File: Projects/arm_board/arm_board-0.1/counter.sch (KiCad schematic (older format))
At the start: 4 parts, among them U1 74HC193, U2 74HC193, U3 74HC193, U4 74HC193

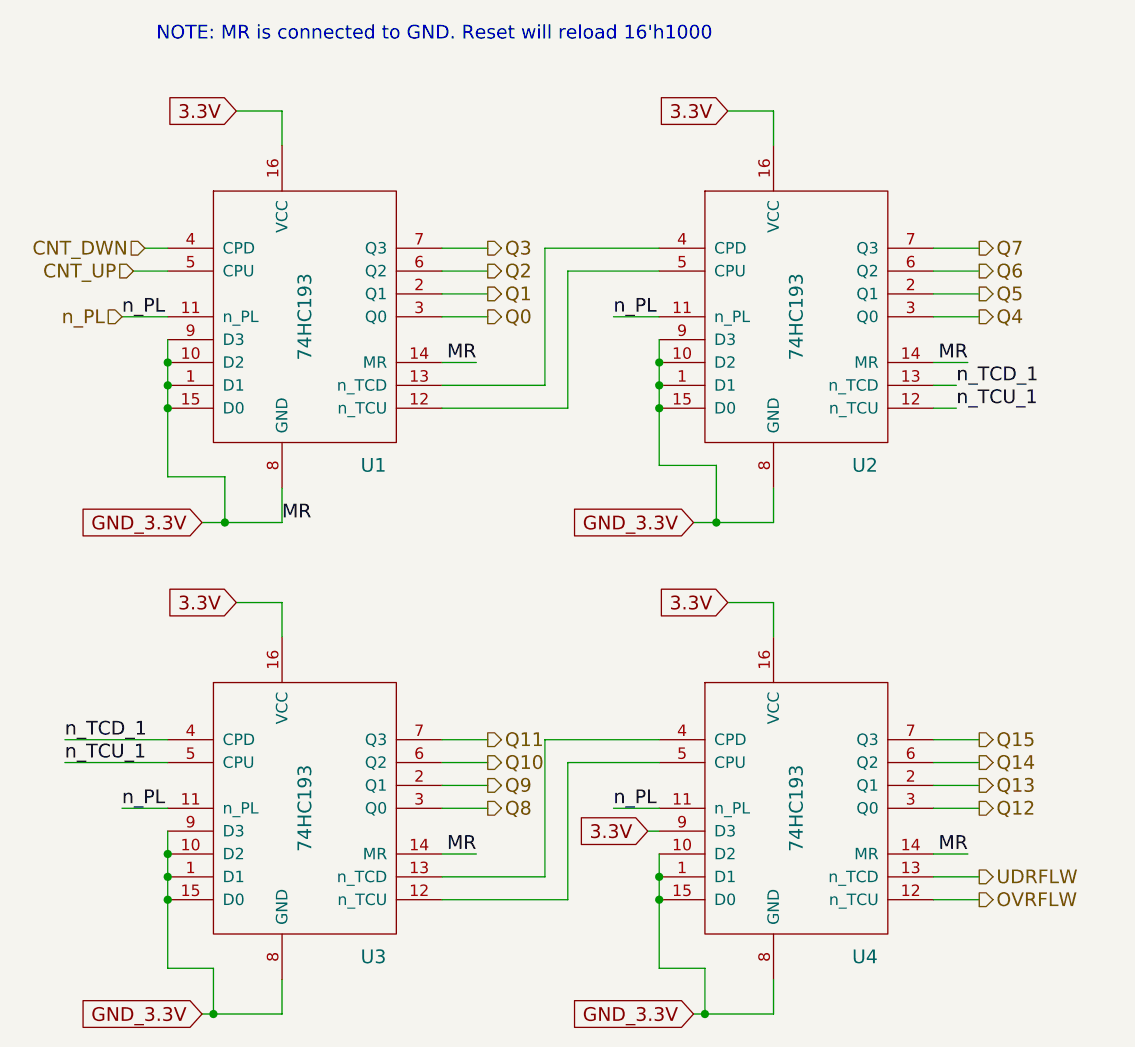
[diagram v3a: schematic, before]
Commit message: Arm Board: bug fixes, and added footprints
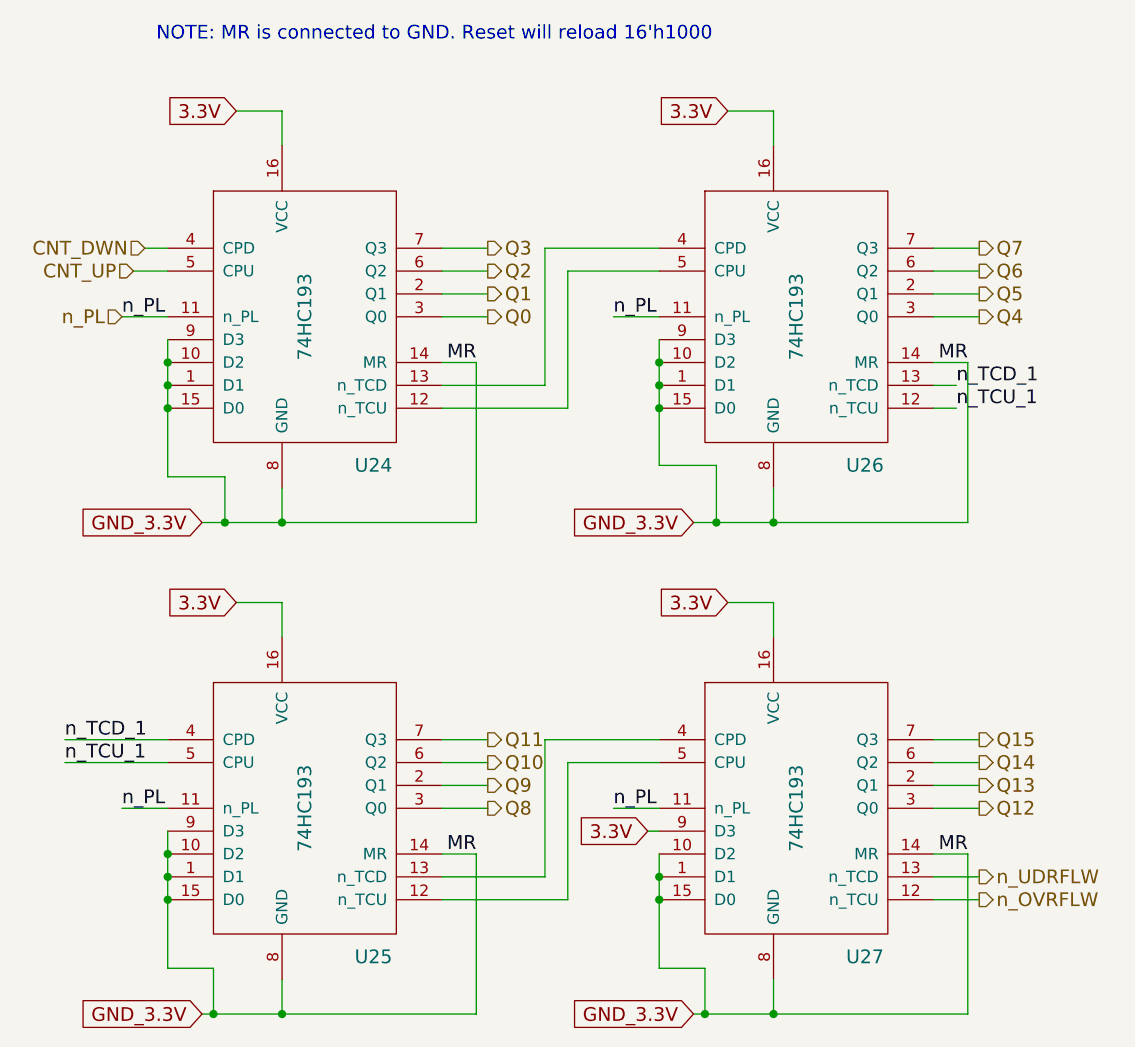
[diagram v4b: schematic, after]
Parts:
- U17: renamed from U1; footprint (none) -> SMD_Packages:SO-16-N
- U18: renamed from U3; footprint (none) -> SMD_Packages:SO-16-N
- U19: renamed from U2; footprint (none) -> SMD_Packages:SO-16-N
- U20: renamed from U4; footprint (none) -> SMD_Packages:SO-16-N
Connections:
- net OVRFLW renamed n_OVRFLW
- net UDRFLW renamed n_UDRFLW
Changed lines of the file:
@@
 LIBS:ArmComponentLibrary
 LIBS:arm_board-cache
-EELAYER 27 0
+EELAYER 25 0
 EELAYER END
 $Descr A4 11693 8268
@@
 $EndDescr
 $Comp
-L 74HC193 U1
+L 74HC193 U17
 U 1 1 564D42F4
 P 4500 2250
-AR Path="/564B31DF/564A908F/564D3AE9/564D42F4" Ref="U1"  Part="1"
-AR Path="/564B31DF/564A908F/564EF627/564D42F4" Ref="U1"  Part="1"
-AR Path="/56666F75/564A908F/564D3AE9/564D42F4" Ref="U1"  Part="1"
-AR Path="/56669634/564A908F/564D3AE9/564D42F4" Ref="U1"  Part="1"
-AR Path="/56669644/564A908F/564D3AE9/564D42F4" Ref="U1"  Part="1"
-AR Path="/5666D2E0/564A908F/564D3AE9/564D42F4" Ref="U1"  Part="1"
-AR Path="/5666D2F0/564A908F/564D3AE9/564D42F4" Ref="U1"  Part="1"
-AR Path="/56F53B7D/564A908F/564D3AE9/564D42F4" Ref="U1"  Part="1"
-AR Path="/56F75F1F/564A908F/564D3AE9/564D42F4" Ref="U1"  Part="1"
-F 0 "U1" H 4800 1600 60  0000 C CNN
+AR Path="/56F5245F/564A908F/564D3AE9/564D42F4" Ref="U17"  Part="1"
+AR Path="/56F53B7D/564A908F/564D3AE9/564D42F4" Ref="U24"  Part="1"
+AR Path="/56F544AF/564A908F/564D3AE9/564D42F4" Ref="U31"  Part="1"
+AR Path="/56F55E0D/564A908F/564D3AE9/564D42F4" Ref="U38"  Part="1"
+AR Path="/56F56B2F/564A908F/564D3AE9/564D42F4" Ref="U45"  Part="1"
+AR Path="/56F75F1F/56AED673/564D3AE9/564D42F4" Ref="U52"  Part="1"
+F 0 "U24" H 4800 1600 60  0000 C CNN
 F 1 "74HC193" V 4500 2250 60  0000 C CNN
-F 2 "" H 4500 2050 60  0000 C CNN
+F 2 "SMD_Packages:SO-16-N" H 4500 2050 60  0001 C CNN
 F 3 "" H 4500 2050 60  0000 C CNN
 	1    4500 2250
@@
 GND_3.3V
 Wire Wire Line
-	4050 3150 4400 3150
+	4050 3150 5250 3150
 Wire Wire Line
 	4400 3150 4400 3000
@@
 	4400 1350 4400 1500
 $Comp
-L 74HC193 U2
+L 74HC193 U19
 U 1 1 564D42F6
 P 6650 2250
-AR Path="/564B31DF/564A908F/564D3AE9/564D42F6" Ref="U2"  Part="1"
-AR Path="/564B31DF/564A908F/564EF627/564D42F6" Ref="U2"  Part="1"
-AR Path="/56666F75/564A908F/564D3AE9/564D42F6" Ref="U2"  Part="1"
-AR Path="/56669634/564A908F/564D3AE9/564D42F6" Ref="U2"  Part="1"
-AR Path="/56669644/564A908F/564D3AE9/564D42F6" Ref="U2"  Part="1"
-AR Path="/5666D2E0/564A908F/564D3AE9/564D42F6" Ref="U2"  Part="1"
-AR Path="/5666D2F0/564A908F/564D3AE9/564D42F6" Ref="U2"  Part="1"
-AR Path="/56F53B7D/564A908F/564D3AE9/564D42F6" Ref="U2"  Part="1"
-AR Path="/56F75F1F/564A908F/564D3AE9/564D42F6" Ref="U2"  Part="1"
-F 0 "U2" H 6950 1600 60  0000 C CNN
+AR Path="/56F5245F/564A908F/564D3AE9/564D42F6" Ref="U19"  Part="1"
+AR Path="/56F53B7D/564A908F/564D3AE9/564D42F6" Ref="U26"  Part="1"
+AR Path="/56F544AF/564A908F/564D3AE9/564D42F6" Ref="U33"  Part="1"
+AR Path="/56F55E0D/564A908F/564D3AE9/564D42F6" Ref="U40"  Part="1"
+AR Path="/56F56B2F/564A908F/564D3AE9/564D42F6" Ref="U47"  Part="1"
+AR Path="/56F75F1F/56AED673/564D3AE9/564D42F6" Ref="U54"  Part="1"
+F 0 "U26" H 6950 1600 60  0000 C CNN
 F 1 "74HC193" V 6650 2250 60  0000 C CNN
-F 2 "" H 6650 2050 60  0000 C CNN
+F 2 "SMD_Packages:SO-16-N" H 6650 2050 60  0001 C CNN
 F 3 "" H 6650 2050 60  0000 C CNN
 	1    6650 2250
@@
 GND_3.3V
 Wire Wire Line
-	6200 3150 6550 3150
+	6200 3150 7400 3150
 Wire Wire Line
 	6550 3150 6550 3000
@@
 	5550 1950 6050 1950
 $Comp
-L 74HC193 U3
+L 74HC193 U18
 U 1 1 564D42F7
 P 4500 4400
-AR Path="/564B31DF/564A908F/564D3AE9/564D42F7" Ref="U3"  Part="1"
-AR Path="/564B31DF/564A908F/564EF627/564D42F7" Ref="U3"  Part="1"
-AR Path="/56666F75/564A908F/564D3AE9/564D42F7" Ref="U3"  Part="1"
-AR Path="/56669634/564A908F/564D3AE9/564D42F7" Ref="U3"  Part="1"
-AR Path="/56669644/564A908F/564D3AE9/564D42F7" Ref="U3"  Part="1"
-AR Path="/5666D2E0/564A908F/564D3AE9/564D42F7" Ref="U3"  Part="1"
-AR Path="/5666D2F0/564A908F/564D3AE9/564D42F7" Ref="U3"  Part="1"
-AR Path="/56F53B7D/564A908F/564D3AE9/564D42F7" Ref="U3"  Part="1"
-AR Path="/56F75F1F/564A908F/564D3AE9/564D42F7" Ref="U3"  Part="1"
-F 0 "U3" H 4800 3750 60  0000 C CNN
+AR Path="/56F5245F/564A908F/564D3AE9/564D42F7" Ref="U18"  Part="1"
+AR Path="/56F53B7D/564A908F/564D3AE9/564D42F7" Ref="U25"  Part="1"
+AR Path="/56F544AF/564A908F/564D3AE9/564D42F7" Ref="U32"  Part="1"
+AR Path="/56F55E0D/564A908F/564D3AE9/564D42F7" Ref="U39"  Part="1"
+AR Path="/56F56B2F/564A908F/564D3AE9/564D42F7" Ref="U46"  Part="1"
+AR Path="/56F75F1F/56AED673/564D3AE9/564D42F7" Ref="U53"  Part="1"
+F 0 "U25" H 4800 3750 60  0000 C CNN
 F 1 "74HC193" V 4500 4400 60  0000 C CNN
-F 2 "" H 4500 4200 60  0000 C CNN
+F 2 "SMD_Packages:SO-16-N" H 4500 4200 60  0001 C CNN
 F 3 "" H 4500 4200 60  0000 C CNN
 	1    4500 4400
@@
 GND_3.3V
 Wire Wire Line
-	4050 5300 4400 5300
+	4050 5300 5250 5300
 Wire Wire Line
 	4400 5300 4400 5150
@@
 	4400 3500 4400 3650
 $Comp
-L 74HC193 U4
+L 74HC193 U20
 U 1 1 564D42F8
 P 6650 4400
-AR Path="/564B31DF/564A908F/564D3AE9/564D42F8" Ref="U4"  Part="1"
-AR Path="/564B31DF/564A908F/564EF627/564D42F8" Ref="U4"  Part="1"
-AR Path="/56666F75/564A908F/564D3AE9/564D42F8" Ref="U4"  Part="1"
-AR Path="/56669634/564A908F/564D3AE9/564D42F8" Ref="U4"  Part="1"
-AR Path="/56669644/564A908F/564D3AE9/564D42F8" Ref="U4"  Part="1"
-AR Path="/5666D2E0/564A908F/564D3AE9/564D42F8" Ref="U4"  Part="1"
-AR Path="/5666D2F0/564A908F/564D3AE9/564D42F8" Ref="U4"  Part="1"
-AR Path="/56F53B7D/564A908F/564D3AE9/564D42F8" Ref="U4"  Part="1"
-AR Path="/56F75F1F/564A908F/564D3AE9/564D42F8" Ref="U4"  Part="1"
-F 0 "U4" H 6950 3750 60  0000 C CNN
+AR Path="/56F5245F/564A908F/564D3AE9/564D42F8" Ref="U20"  Part="1"
+AR Path="/56F53B7D/564A908F/564D3AE9/564D42F8" Ref="U27"  Part="1"
+AR Path="/56F544AF/564A908F/564D3AE9/564D42F8" Ref="U34"  Part="1"
+AR Path="/56F55E0D/564A908F/564D3AE9/564D42F8" Ref="U41"  Part="1"
+AR Path="/56F56B2F/564A908F/564D3AE9/564D42F8" Ref="U48"  Part="1"
+AR Path="/56F75F1F/56AED673/564D3AE9/564D42F8" Ref="U55"  Part="1"
+F 0 "U27" H 6950 3750 60  0000 C CNN
 F 1 "74HC193" V 6650 4400 60  0000 C CNN
-F 2 "" H 6650 4200 60  0000 C CNN
+F 2 "SMD_Packages:SO-16-N" H 6650 4200 60  0001 C CNN
 F 3 "" H 6650 4200 60  0000 C CNN
 	1    6650 4400
@@
 GND_3.3V
 Wire Wire Line
-	6200 5300 6550 5300
+	6200 5300 7400 5300
 Wire Wire Line
 	6550 5300 6550 5150
@@
 	5100 1950 5300 1950
 Text HLabel 7450 4700 2    60   Output ~ 0
-UDRFLW
+n_UDRFLW
 Text HLabel 7450 4800 2    60   Output ~ 0
-OVRFLW
+n_OVRFLW
 Wire Wire Line
 	7450 4800 7250 4800
@@
 Connection ~ 6300 3150
 Connection ~ 6050 2650
-Text Label 4400 3150 0    60   ~ 0
-MR
 Text Notes 3850 1050 0    60   ~ 0
 NOTE: MR is connected to GND. Reset will reload 16'h1000
+Wire Wire Line
+	5250 3150 5250 2450
+Connection ~ 4400 3150
+Wire Wire Line
+	7400 3150 7400 2450
+Connection ~ 6550 3150
+Wire Wire Line
+	5250 5300 5250 4600
+Connection ~ 4400 5300
+Wire Wire Line
+	7400 5300 7400 4600
+Connection ~ 6550 5300
 $EndSCHEMATC

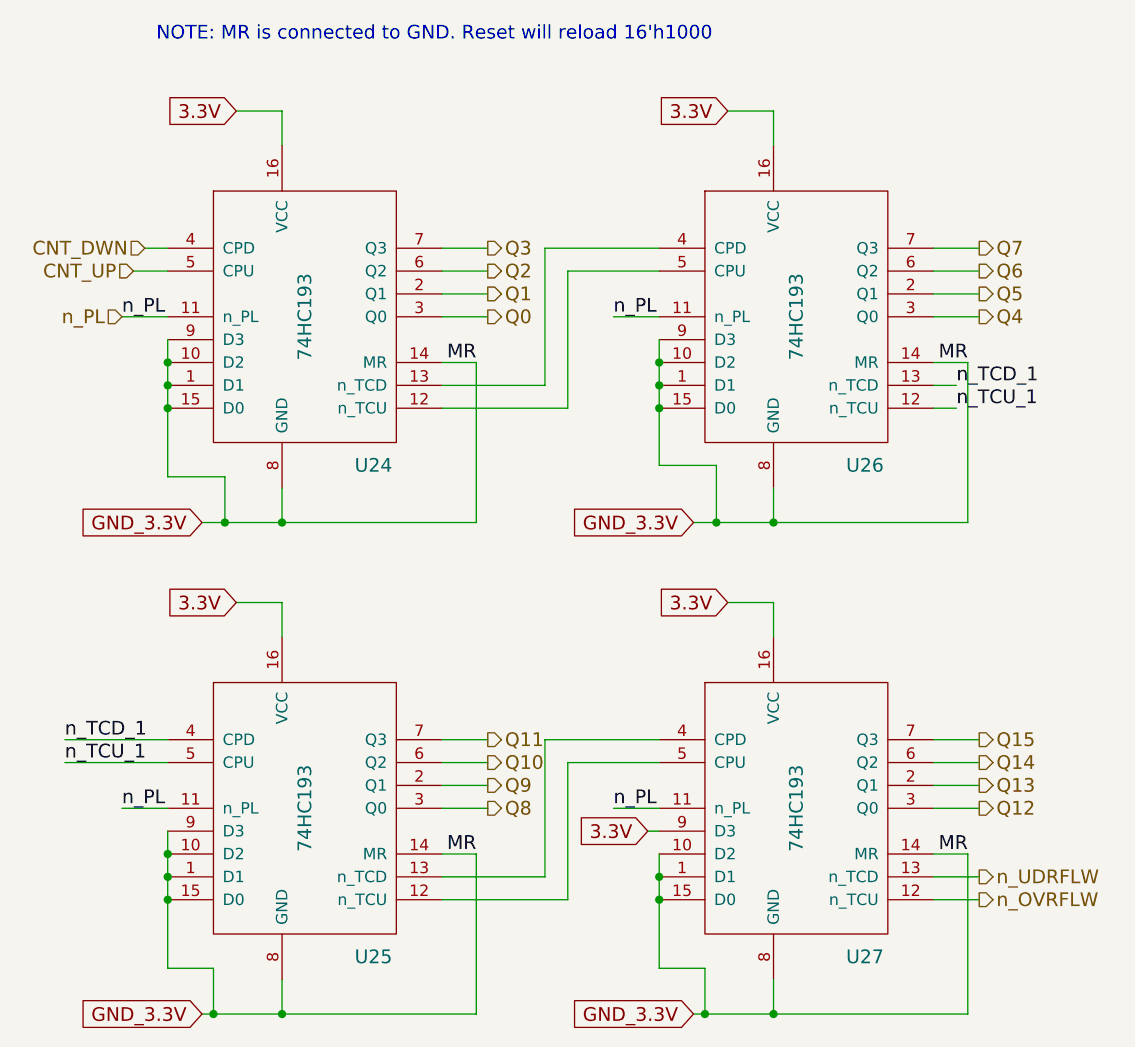
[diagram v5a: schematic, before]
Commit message: Arm Board: finalizing footprints.
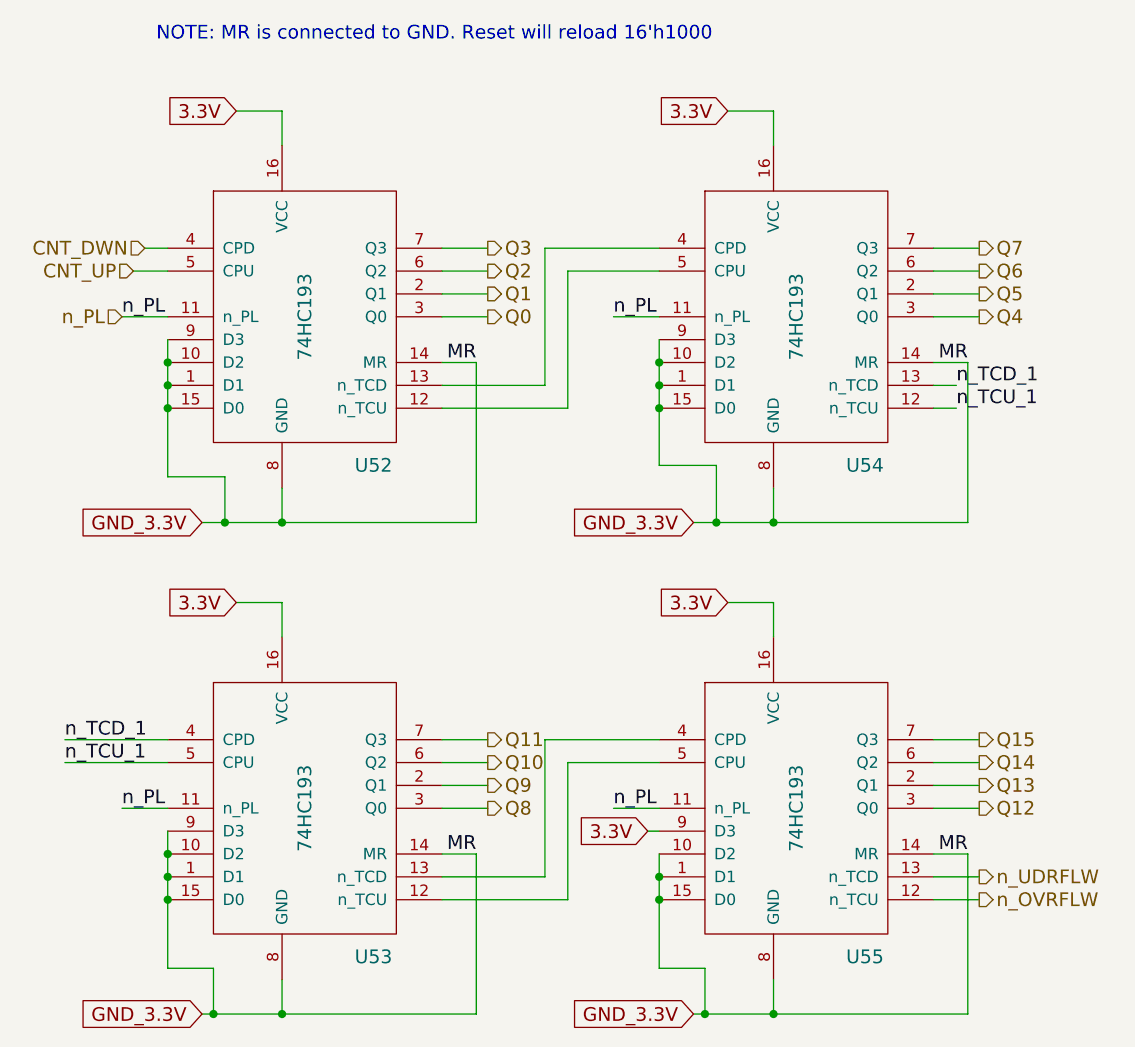
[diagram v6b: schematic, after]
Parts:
- U17, U18, U19, U20: footprint SMD_Packages:SO-16-N -> ArmFootprints:SOIC-16
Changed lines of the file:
@@
 AR Path="/56F56B2F/564A908F/564D3AE9/564D42F4" Ref="U45"  Part="1"
 AR Path="/56F75F1F/56AED673/564D3AE9/564D42F4" Ref="U52"  Part="1"
-F 0 "U24" H 4800 1600 60  0000 C CNN
+F 0 "U52" H 4800 1600 60  0000 C CNN
 F 1 "74HC193" V 4500 2250 60  0000 C CNN
-F 2 "SMD_Packages:SO-16-N" H 4500 2050 60  0001 C CNN
+F 2 "ArmFootprints:SOIC-16" H 4500 2050 60  0001 C CNN
 F 3 "" H 4500 2050 60  0000 C CNN
 	1    4500 2250
@@
 AR Path="/56F56B2F/564A908F/564D3AE9/564D42F6" Ref="U47"  Part="1"
 AR Path="/56F75F1F/56AED673/564D3AE9/564D42F6" Ref="U54"  Part="1"
-F 0 "U26" H 6950 1600 60  0000 C CNN
+F 0 "U54" H 6950 1600 60  0000 C CNN
 F 1 "74HC193" V 6650 2250 60  0000 C CNN
-F 2 "SMD_Packages:SO-16-N" H 6650 2050 60  0001 C CNN
+F 2 "ArmFootprints:SOIC-16" H 6650 2050 60  0001 C CNN
 F 3 "" H 6650 2050 60  0000 C CNN
 	1    6650 2250
@@
 AR Path="/56F56B2F/564A908F/564D3AE9/564D42F7" Ref="U46"  Part="1"
 AR Path="/56F75F1F/56AED673/564D3AE9/564D42F7" Ref="U53"  Part="1"
-F 0 "U25" H 4800 3750 60  0000 C CNN
+F 0 "U53" H 4800 3750 60  0000 C CNN
 F 1 "74HC193" V 4500 4400 60  0000 C CNN
-F 2 "SMD_Packages:SO-16-N" H 4500 4200 60  0001 C CNN
+F 2 "ArmFootprints:SOIC-16" H 4500 4200 60  0001 C CNN
 F 3 "" H 4500 4200 60  0000 C CNN
 	1    4500 4400
@@
 AR Path="/56F56B2F/564A908F/564D3AE9/564D42F8" Ref="U48"  Part="1"
 AR Path="/56F75F1F/56AED673/564D3AE9/564D42F8" Ref="U55"  Part="1"
-F 0 "U27" H 6950 3750 60  0000 C CNN
+F 0 "U55" H 6950 3750 60  0000 C CNN
 F 1 "74HC193" V 6650 4400 60  0000 C CNN
-F 2 "SMD_Packages:SO-16-N" H 6650 4200 60  0001 C CNN
+F 2 "ArmFootprints:SOIC-16" H 6650 4200 60  0001 C CNN
 F 3 "" H 6650 4200 60  0000 C CNN
 	1    6650 4400

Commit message: Arm Board: finish pcb layout, make gerbers
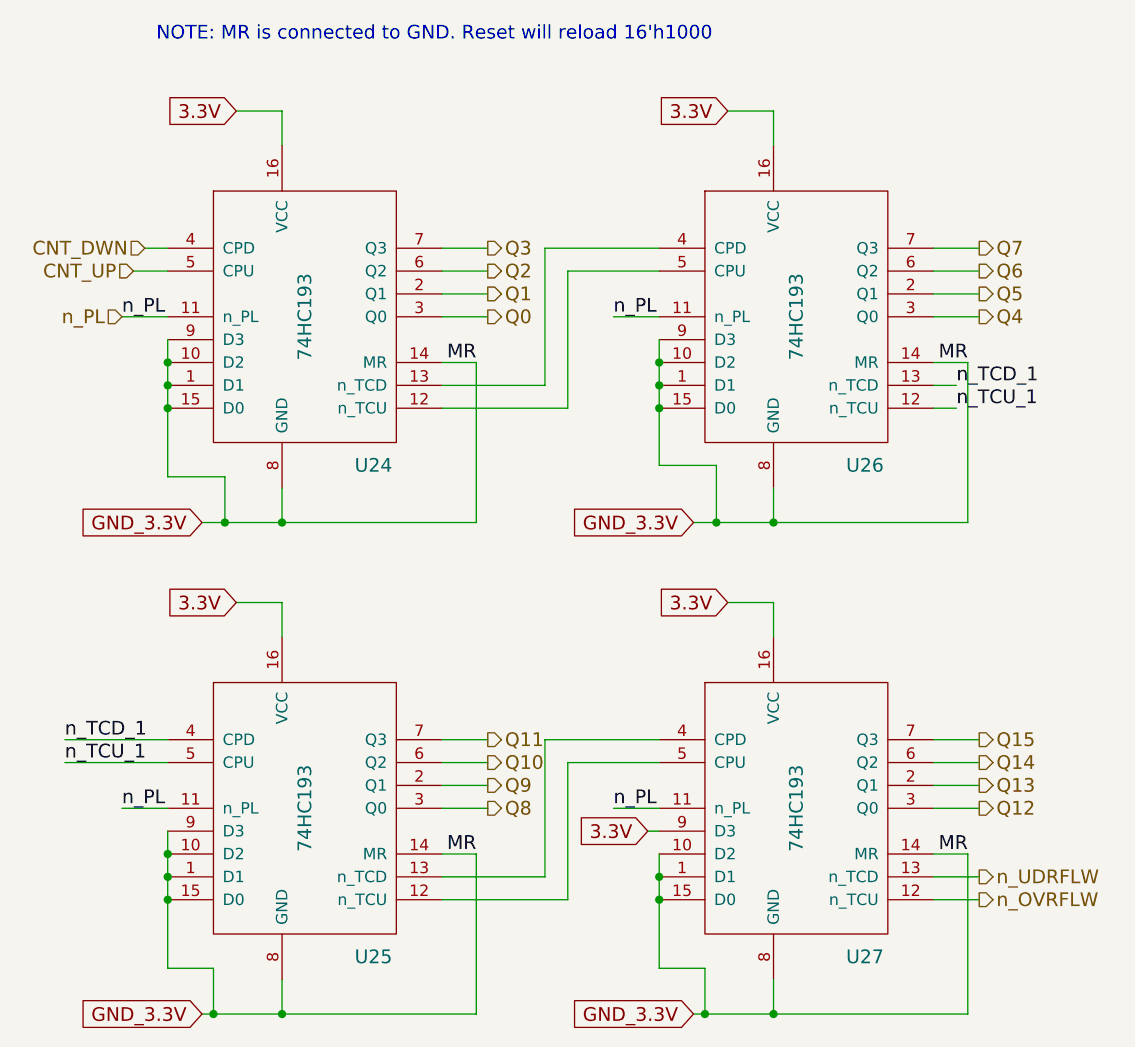
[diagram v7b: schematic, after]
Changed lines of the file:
@@
 AR Path="/56F56B2F/564A908F/564D3AE9/564D42F4" Ref="U45"  Part="1"
 AR Path="/56F75F1F/56AED673/564D3AE9/564D42F4" Ref="U52"  Part="1"
-F 0 "U52" H 4800 1600 60  0000 C CNN
+F 0 "U24" H 4800 1600 60  0000 C CNN
 F 1 "74HC193" V 4500 2250 60  0000 C CNN
 F 2 "ArmFootprints:SOIC-16" H 4500 2050 60  0001 C CNN
@@
 AR Path="/56F56B2F/564A908F/564D3AE9/564D42F6" Ref="U47"  Part="1"
 AR Path="/56F75F1F/56AED673/564D3AE9/564D42F6" Ref="U54"  Part="1"
-F 0 "U54" H 6950 1600 60  0000 C CNN
+F 0 "U26" H 6950 1600 60  0000 C CNN
 F 1 "74HC193" V 6650 2250 60  0000 C CNN
 F 2 "ArmFootprints:SOIC-16" H 6650 2050 60  0001 C CNN
@@
 AR Path="/56F56B2F/564A908F/564D3AE9/564D42F7" Ref="U46"  Part="1"
 AR Path="/56F75F1F/56AED673/564D3AE9/564D42F7" Ref="U53"  Part="1"
-F 0 "U53" H 4800 3750 60  0000 C CNN
+F 0 "U25" H 4800 3750 60  0000 C CNN
 F 1 "74HC193" V 4500 4400 60  0000 C CNN
 F 2 "ArmFootprints:SOIC-16" H 4500 4200 60  0001 C CNN
@@
 AR Path="/56F56B2F/564A908F/564D3AE9/564D42F8" Ref="U48"  Part="1"
 AR Path="/56F75F1F/56AED673/564D3AE9/564D42F8" Ref="U55"  Part="1"
-F 0 "U55" H 6950 3750 60  0000 C CNN
+F 0 "U27" H 6950 3750 60  0000 C CNN
 F 1 "74HC193" V 6650 4400 60  0000 C CNN
 F 2 "ArmFootprints:SOIC-16" H 6650 4200 60  0001 C CNN
